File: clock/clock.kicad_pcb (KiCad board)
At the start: 2 copper layers, 176.8 x 81.3 mm, 136 parts, among them P101 CONN_01X03, P102 CONN_FAN_PWM, P103 CONN_02X08, P301 MCRF, Q201 MMBT3904, U201 PCA9306, U202 DAC8830, U203 LMV722, U204 LTC2990, U205 LP3853, U206 NC7SZ125, U207 NC7SZ125, U301 Adafruit746, U302 MIC5225, U303 PA6H, U401 74LVC541, U501 TPS56428, U502 TPS56428, U503 TPS56428, U601 ADT7410, U602 DS3231, U603 ADT7410, Y201 FVXO-HC53, Y202 CX210

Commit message: Place the reference designators.
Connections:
- P101 pad 3: Net-(P101-Pad3) -> /power/+5V_ENA
- P103 pad 2: GND -> /microzed/~CARRIER_SRST~
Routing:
- net /power/+5V_ENA: track 2.03 -> 136.9 mm, vias 0 -> 2
- net /microzed/~CARRIER_SRST~: track 0.00 -> 61.0 mm, vias 0 -> 3
- net /power/+12V: track 181.5 -> 189.8 mm
- net /microzed/+5V_PG: track 142.2 -> 141.7 mm
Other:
- net class Default: clearance 0.253746 -> 0.254
- rule trace_clearance: 0.253746 -> 0.254

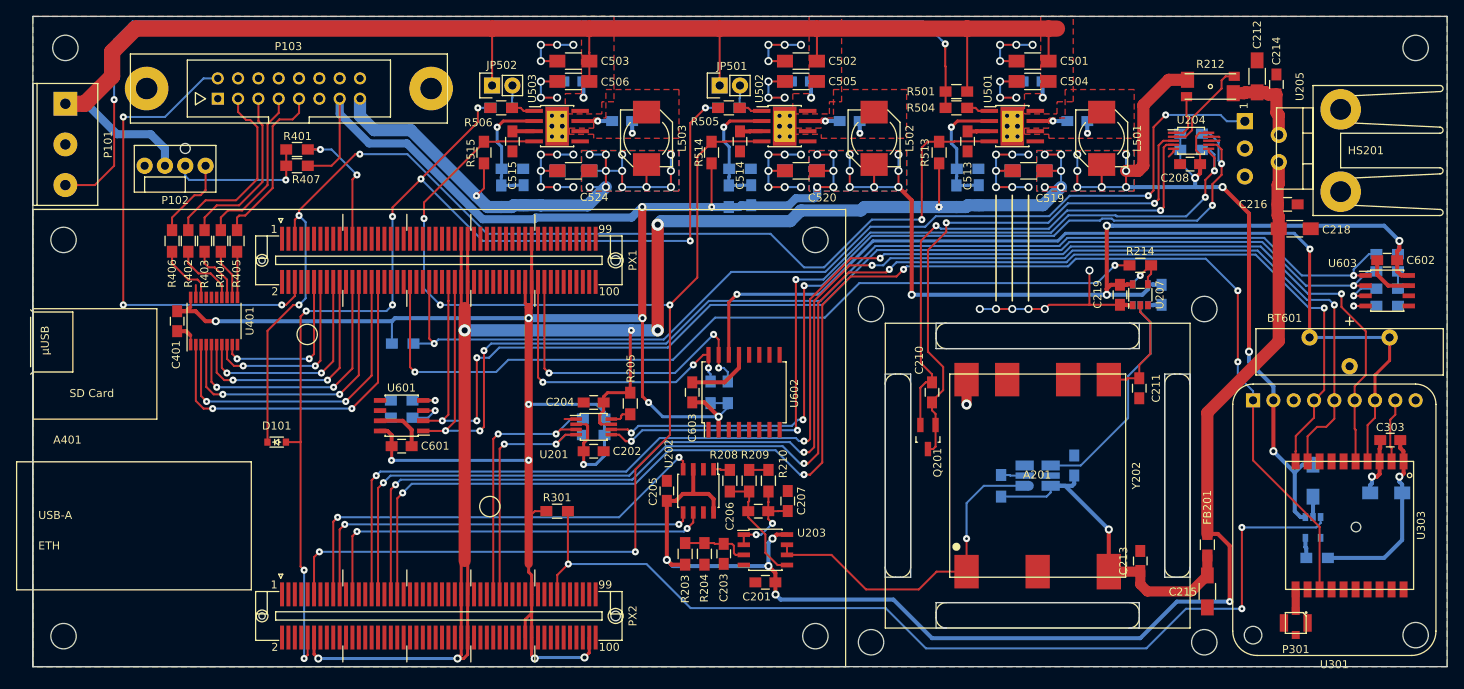
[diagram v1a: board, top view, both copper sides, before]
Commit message: Add more via stitching on the GND fills. Add gerber files.
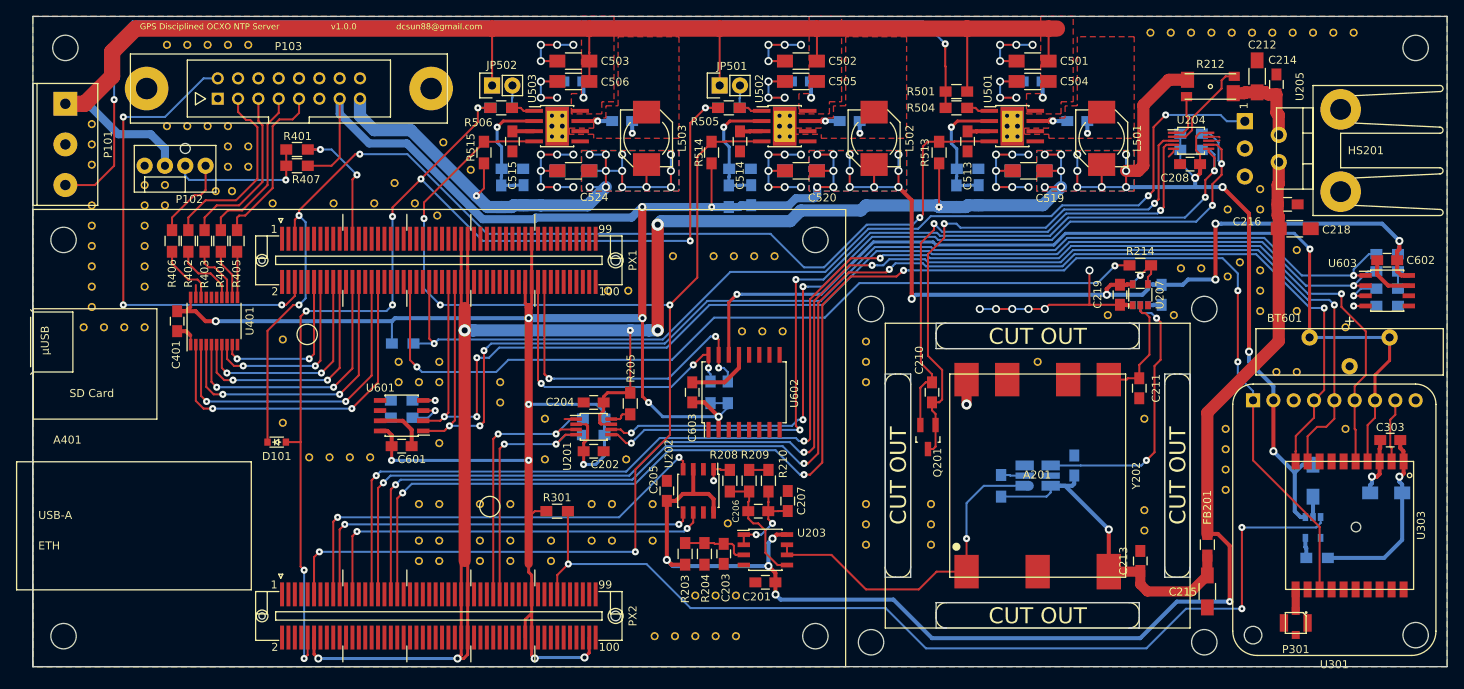
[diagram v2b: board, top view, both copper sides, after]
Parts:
- added REF**: Stiching_Via_40x24mil, local:Stiching_Via_40x24mil, F.Cu at (339.6, 224.3)
- added REF**: Stiching_Via_40x24mil, local:Stiching_Via_40x24mil, F.Cu at (329.4, 226.8)
- added REF**: Stiching_Via_40x24mil, local:Stiching_Via_40x24mil, F.Cu at (348.5, 201.9)
- added REF**: Stiching_Via_40x24mil, local:Stiching_Via_40x24mil, F.Cu at (334.0, 196.6)
- added REF**: Stiching_Via_40x24mil, local:Stiching_Via_40x24mil, F.Cu at (336.6, 196.6)
- added REF**: Stiching_Via_40x24mil, local:Stiching_Via_40x24mil, F.Cu at (339.9, 197.6)
- added REF**: Stiching_Via_40x24mil, local:Stiching_Via_40x24mil, F.Cu at (341.4, 195.8)
- added REF**: Stiching_Via_40x24mil, local:Stiching_Via_40x24mil, F.Cu at (343.9, 201.9)
- added REF**: Stiching_Via_40x24mil, local:Stiching_Via_40x24mil, F.Cu at (343.9, 199.4)
- added REF**: Stiching_Via_40x24mil, local:Stiching_Via_40x24mil, F.Cu at (343.9, 196.8)
- added REF**: Stiching_Via_40x24mil, local:Stiching_Via_40x24mil, F.Cu at (343.9, 186.7)
- added REF**: Stiching_Via_40x24mil, local:Stiching_Via_40x24mil, F.Cu at (343.9, 189.2)
- added REF**: Stiching_Via_40x24mil, local:Stiching_Via_40x24mil, F.Cu at (329.4, 229.4)
- added REF**: Stiching_Via_40x24mil, local:Stiching_Via_40x24mil, F.Cu at (339.9, 189.2)
- added REF**: Stiching_Via_40x24mil, local:Stiching_Via_40x24mil, F.Cu at (217.4, 168.7)
- added REF**: Stiching_Via_40x24mil, local:Stiching_Via_40x24mil, F.Cu at (214.9, 168.7)
- added REF**: Stiching_Via_40x24mil, local:Stiching_Via_40x24mil, F.Cu at (212.3, 168.7)
- added REF**: Stiching_Via_40x24mil, local:Stiching_Via_40x24mil, F.Cu at (209.8, 168.7)
- added REF**: Stiching_Via_40x24mil, local:Stiching_Via_40x24mil, F.Cu at (207.3, 168.7)
- added REF**: Stiching_Via_40x24mil, local:Stiching_Via_40x24mil, F.Cu at (207.3, 178.8)
- added REF**: Stiching_Via_40x24mil, local:Stiching_Via_40x24mil, F.Cu at (209.8, 178.8)
- added REF**: Stiching_Via_40x24mil, local:Stiching_Via_40x24mil, F.Cu at (212.3, 178.8)
- added REF**: Stiching_Via_40x24mil, local:Stiching_Via_40x24mil, F.Cu at (214.9, 178.8)
- added REF**: Stiching_Via_40x24mil, local:Stiching_Via_40x24mil, F.Cu at (324.9, 202.4)
- added REF**: Stiching_Via_40x24mil, local:Stiching_Via_40x24mil, F.Cu at (214.9, 181.4)
- added REF**: Stiching_Via_40x24mil, local:Stiching_Via_40x24mil, F.Cu at (217.4, 181.4)
- added REF**: Stiching_Via_40x24mil, local:Stiching_Via_40x24mil, F.Cu at (214.9, 183.9)
- added REF**: Stiching_Via_40x24mil, local:Stiching_Via_40x24mil, F.Cu at (217.4, 183.9)
- added REF**: Stiching_Via_40x24mil, local:Stiching_Via_40x24mil, F.Cu at (215.4, 186.9)
- added REF**: Stiching_Via_40x24mil, local:Stiching_Via_40x24mil, F.Cu at (213.4, 186.9)
- added REF**: Stiching_Via_40x24mil, local:Stiching_Via_40x24mil, F.Cu at (196.8, 204.0)
- added REF**: Stiching_Via_40x24mil, local:Stiching_Via_40x24mil, F.Cu at (199.4, 204.0)
- added REF**: Stiching_Via_40x24mil, local:Stiching_Via_40x24mil, F.Cu at (201.9, 204.0)
- added REF**: Stiching_Via_40x24mil, local:Stiching_Via_40x24mil, F.Cu at (204.5, 204.0)
- added REF**: Stiching_Via_40x24mil, local:Stiching_Via_40x24mil, F.Cu at (333.1, 202.4)
- added REF**: Stiching_Via_40x24mil, local:Stiching_Via_40x24mil, F.Cu at (204.5, 198.9)
- added REF**: Stiching_Via_40x24mil, local:Stiching_Via_40x24mil, F.Cu at (204.5, 196.3)
- added REF**: Stiching_Via_40x24mil, local:Stiching_Via_40x24mil, F.Cu at (204.5, 193.8)
- added REF**: Stiching_Via_40x24mil, local:Stiching_Via_40x24mil, F.Cu at (204.5, 191.3)
- added REF**: Stiching_Via_40x24mil, local:Stiching_Via_40x24mil, F.Cu at (207.0, 188.7)
- added REF**: Stiching_Via_40x24mil, local:Stiching_Via_40x24mil, F.Cu at (207.0, 186.2)
- added REF**: Stiching_Via_40x24mil, local:Stiching_Via_40x24mil, F.Cu at (204.5, 186.2)
- added REF**: Stiching_Via_40x24mil, local:Stiching_Via_40x24mil, F.Cu at (204.5, 188.7)
- added REF**: Stiching_Via_40x24mil, local:Stiching_Via_40x24mil, F.Cu at (197.9, 201.4)
- added REF**: Stiching_Via_40x24mil, local:Stiching_Via_40x24mil, F.Cu at (197.9, 198.9)
- added REF**: Stiching_Via_40x24mil, local:Stiching_Via_40x24mil, F.Cu at (235.7, 185.9)
- added REF**: Stiching_Via_40x24mil, local:Stiching_Via_40x24mil, F.Cu at (197.9, 196.3)
- added REF**: Stiching_Via_40x24mil, local:Stiching_Via_40x24mil, F.Cu at (197.9, 193.8)
- added REF**: Stiching_Via_40x24mil, local:Stiching_Via_40x24mil, F.Cu at (197.9, 191.3)
- added REF**: Stiching_Via_40x24mil, local:Stiching_Via_40x24mil, F.Cu at (197.9, 188.7)
- added REF**: Stiching_Via_40x24mil, local:Stiching_Via_40x24mil, F.Cu at (197.9, 178.6)
- added REF**: Stiching_Via_40x24mil, local:Stiching_Via_40x24mil, F.Cu at (197.9, 183.6)
- added REF**: Stiching_Via_40x24mil, local:Stiching_Via_40x24mil, F.Cu at (197.9, 181.1)
- added REF**: Stiching_Via_40x24mil, local:Stiching_Via_40x24mil, F.Cu at (241.8, 180.8)
- added REF**: Stiching_Via_40x24mil, local:Stiching_Via_40x24mil, F.Cu at (245.2, 184.3)
- added REF**: Stiching_Via_40x24mil, local:Stiching_Via_40x24mil, F.Cu at (277.4, 228.5)
- added REF**: Stiching_Via_40x24mil, local:Stiching_Via_40x24mil, F.Cu at (268.2, 242.6)
- added REF**: Stiching_Via_40x24mil, local:Stiching_Via_40x24mil, F.Cu at (270.8, 242.6)
- added REF**: Stiching_Via_40x24mil, local:Stiching_Via_40x24mil, F.Cu at (339.6, 221.7)
- added REF**: Stiching_Via_40x24mil, local:Stiching_Via_40x24mil, F.Cu at (278.4, 242.6)
- added REF**: Stiching_Via_40x24mil, local:Stiching_Via_40x24mil, F.Cu at (275.8, 242.6)
- added REF**: Stiching_Via_40x24mil, local:Stiching_Via_40x24mil, F.Cu at (273.3, 242.6)
- added REF**: Stiching_Via_40x24mil, local:Stiching_Via_40x24mil, F.Cu at (273.3, 237.5)
- added REF**: Stiching_Via_40x24mil, local:Stiching_Via_40x24mil, F.Cu at (275.8, 237.5)
- added REF**: Stiching_Via_40x24mil, local:Stiching_Via_40x24mil, F.Cu at (278.4, 237.5)
- added REF**: Stiching_Via_40x24mil, local:Stiching_Via_40x24mil, F.Cu at (268.0, 226.1)
- added REF**: Stiching_Via_40x24mil, local:Stiching_Via_40x24mil, F.Cu at (268.0, 230.6)
- added REF**: Stiching_Via_40x24mil, local:Stiching_Via_40x24mil, F.Cu at (264.7, 220.5)
- added REF**: Stiching_Via_40x24mil, local:Stiching_Via_40x24mil, F.Cu at (254.5, 220.5)
- added REF**: Stiching_Via_40x24mil, local:Stiching_Via_40x24mil, F.Cu at (339.6, 219.2)
- added REF**: Stiching_Via_40x24mil, local:Stiching_Via_40x24mil, F.Cu at (254.5, 215.4)
- added REF**: Stiching_Via_40x24mil, local:Stiching_Via_40x24mil, F.Cu at (262.4, 199.4)
- added REF**: Stiching_Via_40x24mil, local:Stiching_Via_40x24mil, F.Cu at (264.9, 199.4)
- added REF**: Stiching_Via_40x24mil, local:Stiching_Via_40x24mil, F.Cu at (220.5, 188.5)
- added REF**: Stiching_Via_40x24mil, local:Stiching_Via_40x24mil, F.Cu at (228.1, 188.5)
- added REF**: Stiching_Via_40x24mil, local:Stiching_Via_40x24mil, F.Cu at (233.2, 188.5)
- added REF**: Stiching_Via_40x24mil, local:Stiching_Via_40x24mil, F.Cu at (238.3, 188.5)
- added REF**: Stiching_Via_40x24mil, local:Stiching_Via_40x24mil, F.Cu at (241.0, 190.0)
- added REF**: Stiching_Via_40x24mil, local:Stiching_Via_40x24mil, F.Cu at (279.1, 204.5)
- added REF**: Stiching_Via_40x24mil, local:Stiching_Via_40x24mil, F.Cu at (270.5, 195.1)
- added REF**: Stiching_Via_40x24mil, local:Stiching_Via_40x24mil, F.Cu at (339.6, 216.7)
- added REF**: Stiching_Via_40x24mil, local:Stiching_Via_40x24mil, F.Cu at (294.6, 231.1)
- added REF**: Stiching_Via_40x24mil, local:Stiching_Via_40x24mil, F.Cu at (294.6, 228.6)
- added REF**: Stiching_Via_40x24mil, local:Stiching_Via_40x24mil, F.Cu at (294.6, 226.1)
- added REF**: Stiching_Via_40x24mil, local:Stiching_Via_40x24mil, F.Cu at (294.6, 210.8)
- added REF**: Stiching_Via_40x24mil, local:Stiching_Via_40x24mil, F.Cu at (294.6, 208.3)
- added REF**: Stiching_Via_40x24mil, local:Stiching_Via_40x24mil, F.Cu at (294.6, 205.7)
- added REF**: Stiching_Via_40x24mil, local:Stiching_Via_40x24mil, F.Cu at (281.7, 204.5)
- added REF**: Stiching_Via_40x24mil, local:Stiching_Via_40x24mil, F.Cu at (284.2, 204.5)
- added REF**: Stiching_Via_40x24mil, local:Stiching_Via_40x24mil, F.Cu at (283.2, 195.1)
- added REF**: Stiching_Via_40x24mil, local:Stiching_Via_40x24mil, F.Cu at (280.7, 195.1)
- added REF**: Stiching_Via_40x24mil, local:Stiching_Via_40x24mil, F.Cu at (316.1, 208.3)
- added REF**: Stiching_Via_40x24mil, local:Stiching_Via_40x24mil, F.Cu at (278.1, 195.1)
- added REF**: Stiching_Via_40x24mil, local:Stiching_Via_40x24mil, F.Cu at (275.6, 195.1)
- added REF**: Stiching_Via_40x24mil, local:Stiching_Via_40x24mil, F.Cu at (260.4, 226.1)
- added REF**: Stiching_Via_40x24mil, local:Stiching_Via_40x24mil, F.Cu at (262.9, 226.1)
- added REF**: Stiching_Via_40x24mil, local:Stiching_Via_40x24mil, F.Cu at (262.9, 230.6)
- added REF**: Stiching_Via_40x24mil, local:Stiching_Via_40x24mil, F.Cu at (260.4, 230.6)
- added REF**: Stiching_Via_40x24mil, local:Stiching_Via_40x24mil, F.Cu at (248.9, 213.4)
- added REF**: Stiching_Via_40x24mil, local:Stiching_Via_40x24mil, F.Cu at (248.9, 210.8)
- added REF**: Stiching_Via_40x24mil, local:Stiching_Via_40x24mil, F.Cu at (232.7, 220.2)
- added REF**: Stiching_Via_40x24mil, local:Stiching_Via_40x24mil, F.Cu at (230.1, 220.2)
- added REF**: Stiching_Via_40x24mil, local:Stiching_Via_40x24mil, F.Cu at (302.8, 231.1)
- added REF**: Stiching_Via_40x24mil, local:Stiching_Via_40x24mil, F.Cu at (227.6, 220.2)
- added REF**: Stiching_Via_40x24mil, local:Stiching_Via_40x24mil, F.Cu at (225.0, 220.2)
- added REF**: Stiching_Via_40x24mil, local:Stiching_Via_40x24mil, F.Cu at (221.7, 215.9)
- added REF**: Stiching_Via_40x24mil, local:Stiching_Via_40x24mil, F.Cu at (221.7, 205.5)
- added REF**: Stiching_Via_40x24mil, local:Stiching_Via_40x24mil, F.Cu at (255.3, 230.6)
- added REF**: Stiching_Via_40x24mil, local:Stiching_Via_40x24mil, F.Cu at (255.3, 233.2)
- added REF**: Stiching_Via_40x24mil, local:Stiching_Via_40x24mil, F.Cu at (250.2, 233.2)
- added REF**: Stiching_Via_40x24mil, local:Stiching_Via_40x24mil, F.Cu at (246.4, 233.2)
- added REF**: Stiching_Via_40x24mil, local:Stiching_Via_40x24mil, F.Cu at (241.3, 233.2)
- added REF**: Stiching_Via_40x24mil, local:Stiching_Via_40x24mil, F.Cu at (238.8, 233.2)
- added REF**: Stiching_Via_40x24mil, local:Stiching_Via_40x24mil, F.Cu at (302.8, 228.6)
- added REF**: Stiching_Via_40x24mil, local:Stiching_Via_40x24mil, F.Cu at (238.8, 230.6)
- added REF**: Stiching_Via_40x24mil, local:Stiching_Via_40x24mil, F.Cu at (241.3, 230.6)
- added REF**: Stiching_Via_40x24mil, local:Stiching_Via_40x24mil, F.Cu at (246.4, 230.6)
- added REF**: Stiching_Via_40x24mil, local:Stiching_Via_40x24mil, F.Cu at (250.2, 230.6)
- added REF**: Stiching_Via_40x24mil, local:Stiching_Via_40x24mil, F.Cu at (250.2, 226.1)
- added REF**: Stiching_Via_40x24mil, local:Stiching_Via_40x24mil, F.Cu at (246.4, 226.1)
- added REF**: Stiching_Via_40x24mil, local:Stiching_Via_40x24mil, F.Cu at (238.8, 226.1)
- added REF**: Stiching_Via_40x24mil, local:Stiching_Via_40x24mil, F.Cu at (241.3, 226.1)
- added REF**: Stiching_Via_40x24mil, local:Stiching_Via_40x24mil, F.Cu at (241.3, 218.4)
- added REF**: Stiching_Via_40x24mil, local:Stiching_Via_40x24mil, F.Cu at (236.2, 208.3)
- added REF**: Stiching_Via_40x24mil, local:Stiching_Via_40x24mil, F.Cu at (302.8, 226.1)
- added REF**: Stiching_Via_40x24mil, local:Stiching_Via_40x24mil, F.Cu at (241.3, 208.3)
- added REF**: Stiching_Via_40x24mil, local:Stiching_Via_40x24mil, F.Cu at (236.2, 210.8)
- added REF**: Stiching_Via_40x24mil, local:Stiching_Via_40x24mil, F.Cu at (238.8, 210.8)
- added REF**: Stiching_Via_40x24mil, local:Stiching_Via_40x24mil, F.Cu at (241.3, 210.8)
- added REF**: Stiching_Via_40x24mil, local:Stiching_Via_40x24mil, F.Cu at (354.6, 216.7)
- added REF**: Stiching_Via_40x24mil, local:Stiching_Via_40x24mil, F.Cu at (354.6, 204.0)
- added REF**: Stiching_Via_40x24mil, local:Stiching_Via_40x24mil, F.Cu at (345.9, 209.6)
- added REF**: Stiching_Via_40x24mil, local:Stiching_Via_40x24mil, F.Cu at (348.5, 209.6)
- added REF**: Stiching_Via_40x24mil, local:Stiching_Via_40x24mil, F.Cu at (355.6, 167.1)
- added REF**: Stiching_Via_40x24mil, local:Stiching_Via_40x24mil, F.Cu at (353.1, 167.1)
- added REF**: Stiching_Via_40x24mil, local:Stiching_Via_40x24mil, F.Cu at (329.4, 215.4)
- added REF**: Stiching_Via_40x24mil, local:Stiching_Via_40x24mil, F.Cu at (350.5, 167.1)
- added REF**: Stiching_Via_40x24mil, local:Stiching_Via_40x24mil, F.Cu at (348.0, 167.1)
- added REF**: Stiching_Via_40x24mil, local:Stiching_Via_40x24mil, F.Cu at (345.4, 167.1)
- added REF**: Stiching_Via_40x24mil, local:Stiching_Via_40x24mil, F.Cu at (342.9, 167.1)
- added REF**: Stiching_Via_40x24mil, local:Stiching_Via_40x24mil, F.Cu at (340.4, 167.1)
- added REF**: Stiching_Via_40x24mil, local:Stiching_Via_40x24mil, F.Cu at (337.8, 167.1)
- added REF**: Stiching_Via_40x24mil, local:Stiching_Via_40x24mil, F.Cu at (335.3, 167.1)
- added REF**: Stiching_Via_40x24mil, local:Stiching_Via_40x24mil, F.Cu at (332.7, 167.1)
- added REF**: Stiching_Via_40x24mil, local:Stiching_Via_40x24mil, F.Cu at (330.2, 167.1)
- added REF**: Stiching_Via_40x24mil, local:Stiching_Via_40x24mil, F.Cu at (348.5, 194.3)
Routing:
- net VCC: track 448.3 -> 441.6 mm, vias 29 -> 30
- net /ocxo/VCXO_10M: track 27.9 -> 34.1 mm, vias 0 -> 2
- net /microzed/+1.8V_PG: track 146.2 -> 149.3 mm
- net /ocxo/DAC_OUT: track 2.07 -> 3.50 mm, vias 0 -> 1
- net /gps/1PPS: track 186.8 -> 188.0 mm
- net /ocxo/TSENSE_A: track 68.2 -> 69.1 mm
- net /microzed/TEMP_SCL: track 158.8 -> 157.9 mm
- net /ocxo/TSENSE_C: track 65.9 -> 66.7 mm
- net /ocxo/SDA5: track 109.3 -> 110.1 mm
- net /microzed/RTC_SDA: track 41.2 -> 42.0 mm
- net /microzed/RTC_SCL: track 38.6 -> 39.3 mm
- net /microzed/TEMP_SDA: track 155.2 -> 154.6 mm
- net /microzed/10MHZ: track 106.4 -> 105.8 mm
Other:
- rule trace_min: 0.1524 -> 0.006
- rule via_min_size: 0.6858 -> 0.027
- board text added: "10MHZ"
- board text added: "1PPS"
- board text added: "3DFX"
- board text added: "CUT OUT"
- board text added: "DAC_OUT"
- board text added: "DAC_SCK"
- board text added: "DAC_SDI"
- board text added: "GPS Disciplined OCXO NTP Server"
- board text added: "GPS_RX"
- board text added: "GPS_TX"
- board text added: "OCXO_SCL"
- board text added: "OCXO_SDA"
- board text added: "SCL5"
- board text added: "SDA5"
- board text added: "TEMP_SCL"
- board text added: "TEMP_SDA"
- board text added: "VC"
- board text added: "VGND_1.65V"
- board text added: "dcsun88@gmail.com"
- board text added: "v1.0.0"
- board text added: "~DAC_CS~"

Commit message: Correct spelling. Minor clean ups.
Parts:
- removed the REF** at (217.4, 168.7)
- removed the REF** at (196.8, 204.0)
- removed the REF** at (204.5, 191.3)
- removed the REF** at (197.9, 201.4)
- removed the REF** at (197.9, 191.3)
- removed the REF** at (197.9, 188.7)
- removed the REF** at (268.2, 242.6)
- removed the REF** at (270.8, 242.6)
- removed the REF** at (348.0, 167.1)
- removed the REF** at (337.8, 167.1)
- added REF**: Stitching_Via_40x24mil, local:Stitching_Via_40x24mil, F.Cu at (363.7, 186.9)
- added REF**: Stitching_Via_40x24mil, local:Stitching_Via_40x24mil, F.Cu at (358.6, 186.9)
- added REF**: Stitching_Via_40x24mil, local:Stitching_Via_40x24mil, F.Cu at (358.6, 176.8)
- added REF**: Stitching_Via_40x24mil, local:Stitching_Via_40x24mil, F.Cu at (363.7, 176.8)
- added REF**: Stitching_Via_40x24mil, local:Stitching_Via_40x24mil, F.Cu at (363.7, 181.9)
- added REF**: Stitching_Via_40x24mil, local:Stitching_Via_40x24mil, F.Cu at (358.6, 181.9)
- REF** (x136): value Stiching_Via_40x24mil -> Stitching_Via_40x24mil; footprint local:Stiching_Via_40x24mil -> local:Stitching_Via_40x24mil
- moved R604 1.14 mm to (276.4, 212.1)
- moved R603 1.02 mm to (278.4, 212.1)
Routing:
- net GND: track 155.2 -> 174.3 mm
- net Net-(U602-Pad1): track 0.00 -> 2.53 mm, vias 0 -> 1
- net VCC: track 441.6 -> 444.0 mm
- net /microzed/RTC_SDA: track 42.0 -> 42.9 mm
- net /microzed/RTC_SCL: track 39.3 -> 40.1 mm
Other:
- board text added: "32KHZ"
- board text added: "BLANK"
- board text added: "LAT"
- board text added: "SCLK"
- board text added: "SIN"

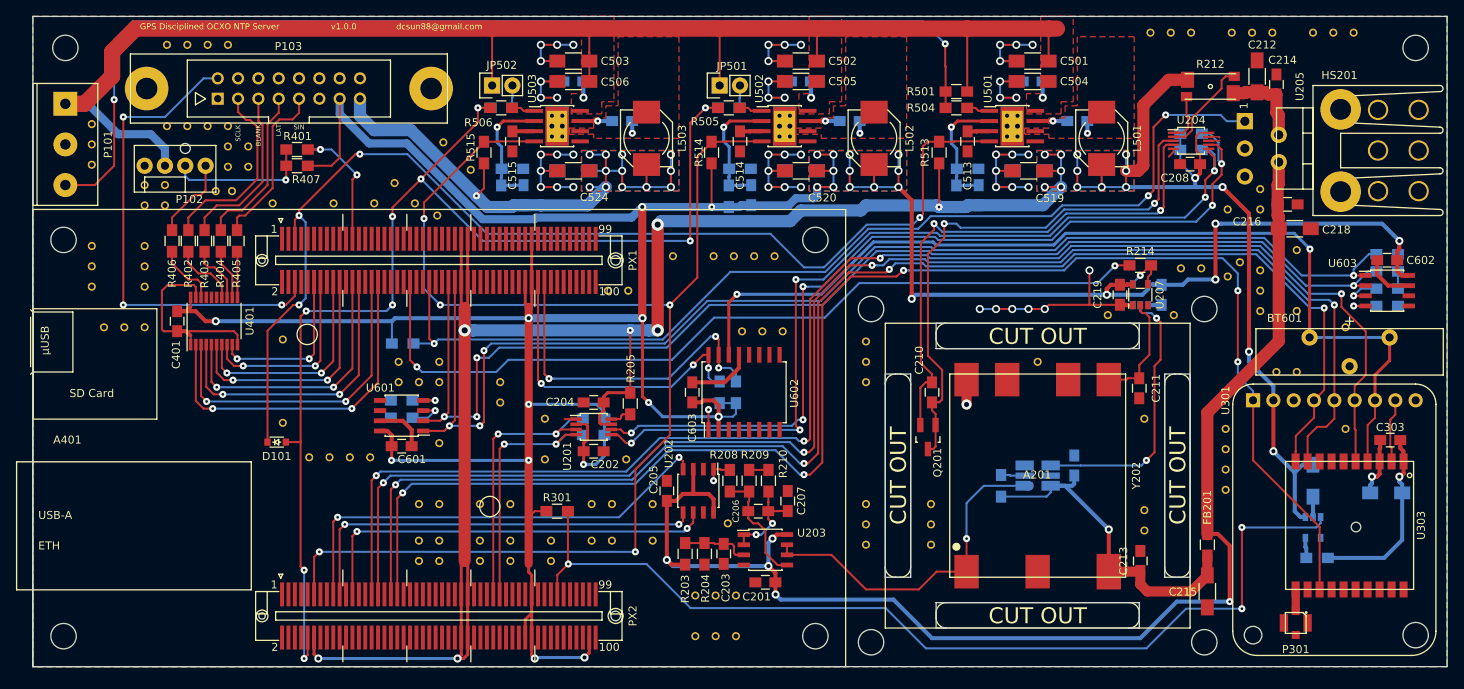
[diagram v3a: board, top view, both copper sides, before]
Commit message: Change SOT-23 footprint. Move some vias onto grid.
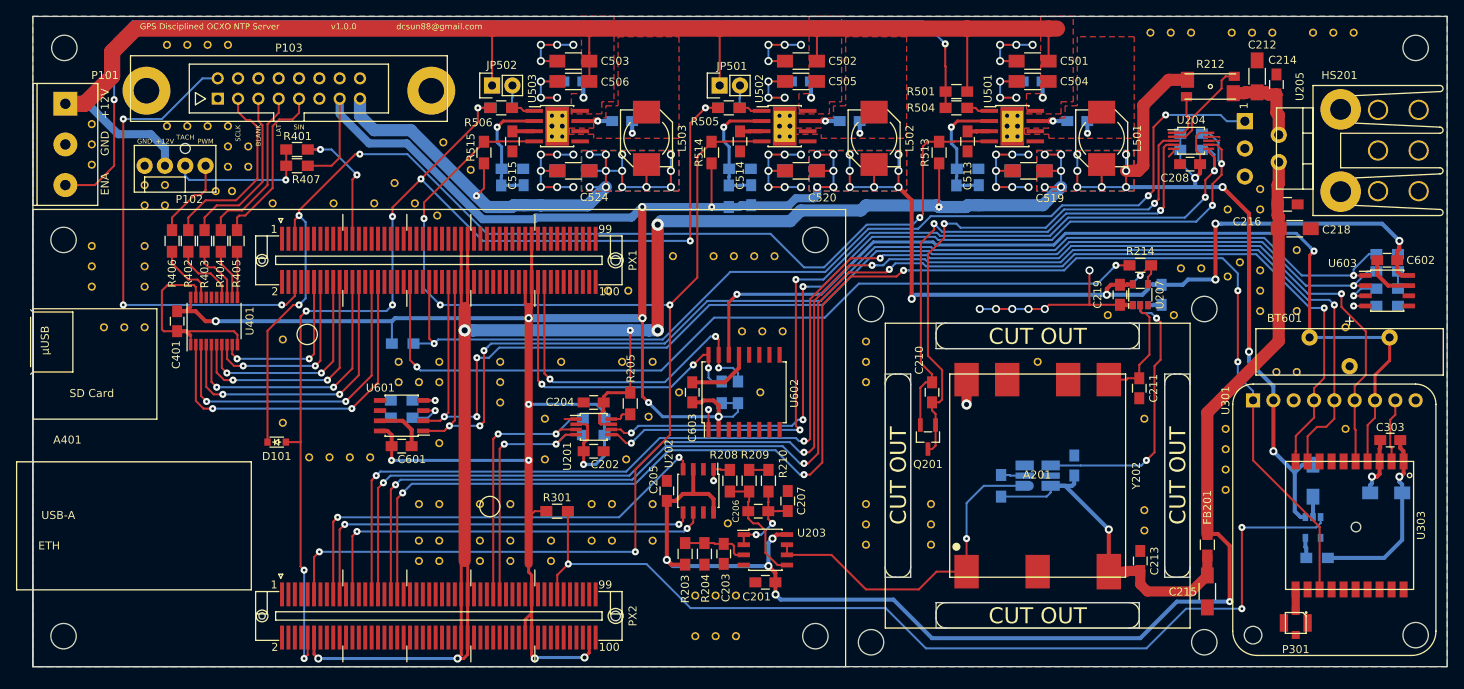
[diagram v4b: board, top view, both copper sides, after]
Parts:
- added REF**: Stitching_Via_40x24mil, local:Stitching_Via_40x24mil, F.Cu at (281.4, 212.1)
- added REF**: Stitching_Via_40x24mil, local:Stitching_Via_40x24mil, F.Cu at (271.3, 212.1)
- added REF**: Stitching_Via_40x24mil, local:Stitching_Via_40x24mil, F.Cu at (267.5, 215.1)
- added REF**: Stitching_Via_40x24mil, local:Stitching_Via_40x24mil, F.Cu at (268.0, 208.3)
- added REF**: Stitching_Via_40x24mil, local:Stitching_Via_40x24mil, F.Cu at (264.2, 208.3)
- added REF**: Stitching_Via_40x24mil, local:Stitching_Via_40x24mil, F.Cu at (256.5, 208.3)
- added REF**: Stitching_Via_40x24mil, local:Stitching_Via_40x24mil, F.Cu at (248.9, 208.3)
- P103: value CONN_02X08 -> XG4A-1631; footprint Connect:he10-16d -> local:XG4A-1631
- Q201: footprint Housings_SOT-23_SOT-143_TSOT-6:SOT-23_Handsoldering -> local:SOT-23-3_NXP_HandSoldering
- moved R604 0.25 mm to (276.6, 212.1)
- moved R603 0.25 mm to (278.6, 212.1)
- moved REF** 0.13 mm to (194.4, 169.0)
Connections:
- P103 pad 0: (no net) -> GND
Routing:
- net /microzed/RTC_SDA: track 42.9 -> 43.5 mm
- net /rtctemp/BATTERY: track 121.6 -> 122.2 mm
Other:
- board text added: "+12V"
- board text added: "ENA"
- board text added: "GND"
- board text added: "PWM"
- board text added: "TACH"

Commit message: Move some vias onto grid.
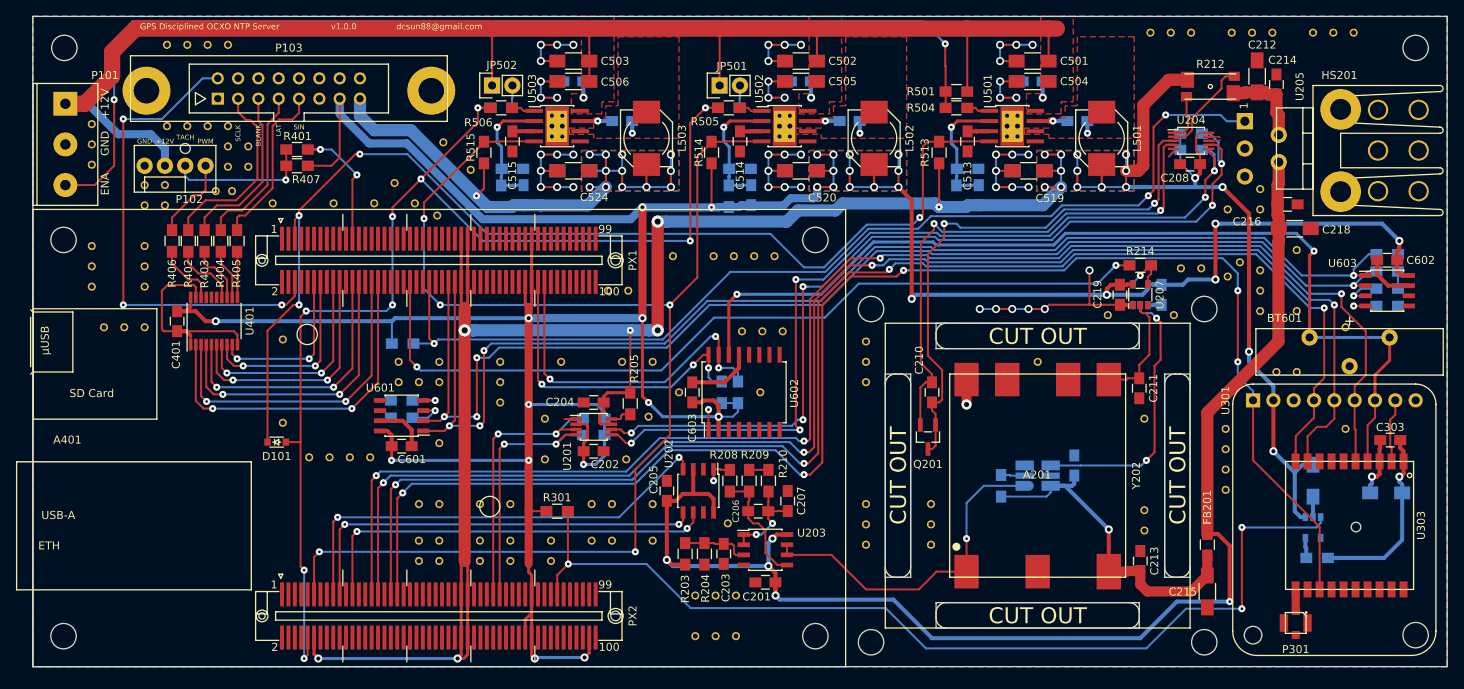
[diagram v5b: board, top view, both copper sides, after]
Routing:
- net /microzed/+5V_PG: track 141.4 -> 140.7 mm
